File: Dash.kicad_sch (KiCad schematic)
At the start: 120 parts, among them J1 Conn_01x03_Socket, J10 Conn_01x03_Socket, J11 Conn_01x04_Socket, J2 Conn_01x03_Socket, J3 Conn_01x03_Socket, J4 Conn_01x03_Socket, J5 Conn_01x03_Socket, J6 Conn_01x03_Socket, J7 Conn_01x07_Socket, J8 Conn_01x06_Socket, J9 Conn_01x05_Socket, Q1 2N7000, Q10 NPN, Q11 NPN, Q12 NPN, Q13 NPN, Q14 NPN, Q15 NPN, Q16 NPN, Q2 NPN, Q3 NPN, Q4 NPN, Q5 NPN, Q6 NPN, Q7 NPN, Q8 NPN, Q9 NPN, SW1 SW_Push, U1 SFH617A-1, U2 24C02Cx-x-SN, U3 24C02Cx-x-SN, U4 LM2678T-3.3, U5 LM2678T-5.0, U6 ESP32-S2-DevKitM

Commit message: Update Dash.kicad_sch
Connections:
- net Brake Out is gone; now on net Brake Adjusted: Q14.1 (C), R41.1
- net Headlights High Out is gone; now on net Headlights High Adjusted: Q8.1 (C), R29.1
- net Headlights Low Out is gone; now on net Headlights Low Adjusted: Q3.1 (C), R45.1
- net Left Turn Out is gone; now on net Left Turn Adjusted: Q9.1 (C), R30.1
- net Right Turn Out is gone; now on net Right Turn Adjusted: Q10.1 (C), R46.1
- net Speed Out is gone; now on net Speed Adjusted: Q5.1 (C), R24.1
- net Tach Out is gone; now on net Tach Adjusted: Q2.1 (C), R10.1
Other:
- moved on the sheet: Q10, Q11, Q12, Q13, Q14, Q15, Q2, Q3, Q4, Q5, Q6, Q7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

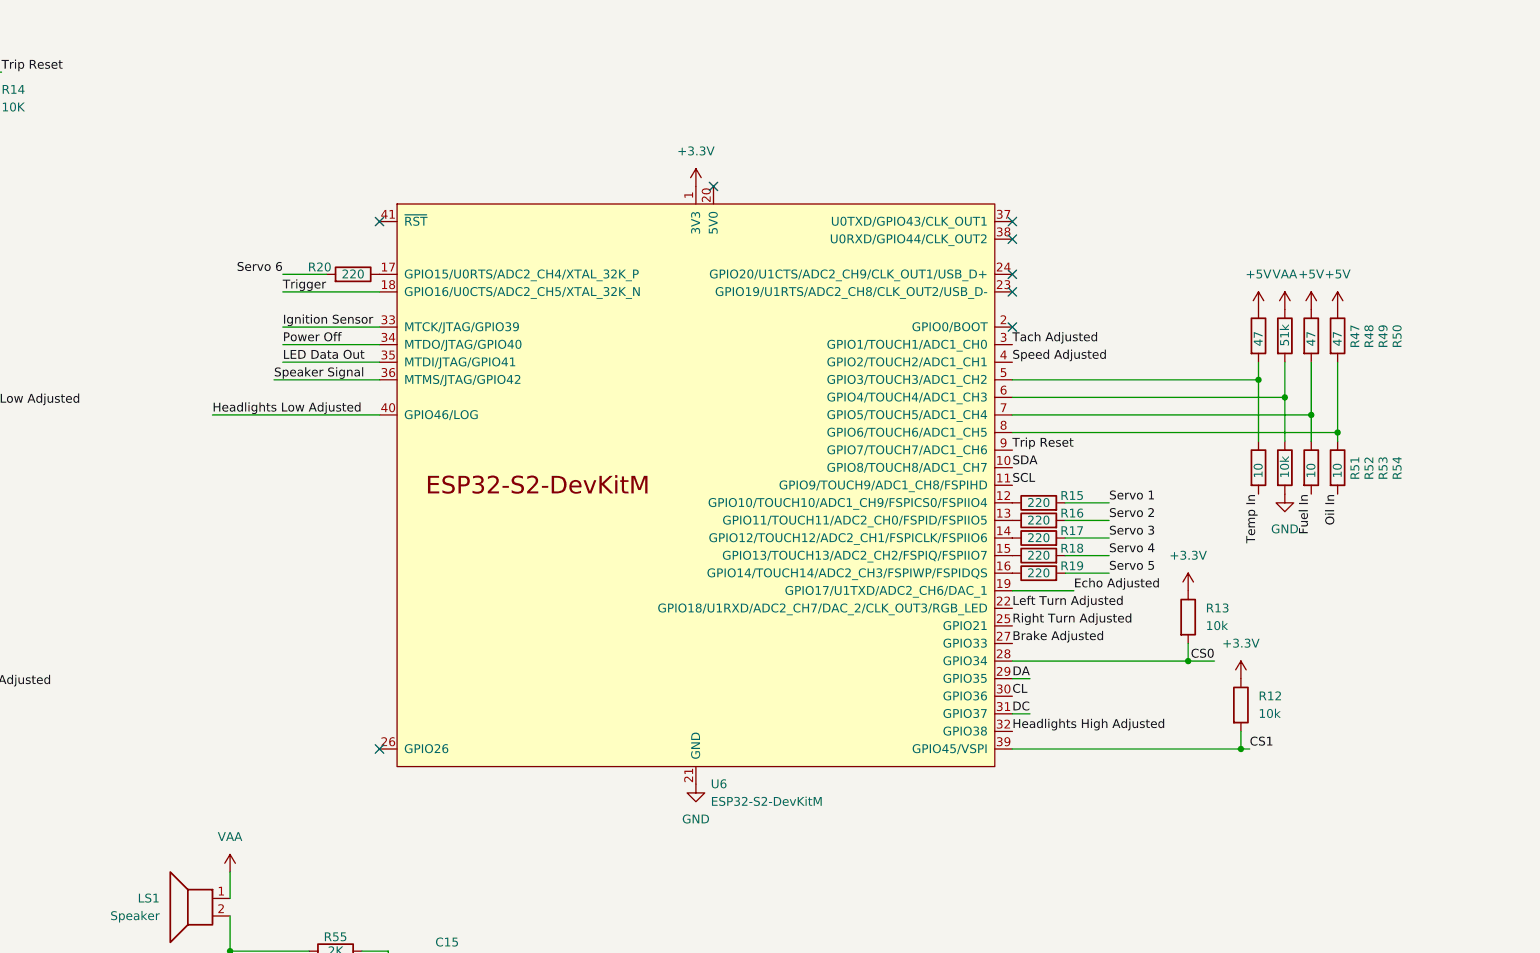
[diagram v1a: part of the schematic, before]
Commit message: added potentiometers
Added potentiometers  to test gauges to the schematic.
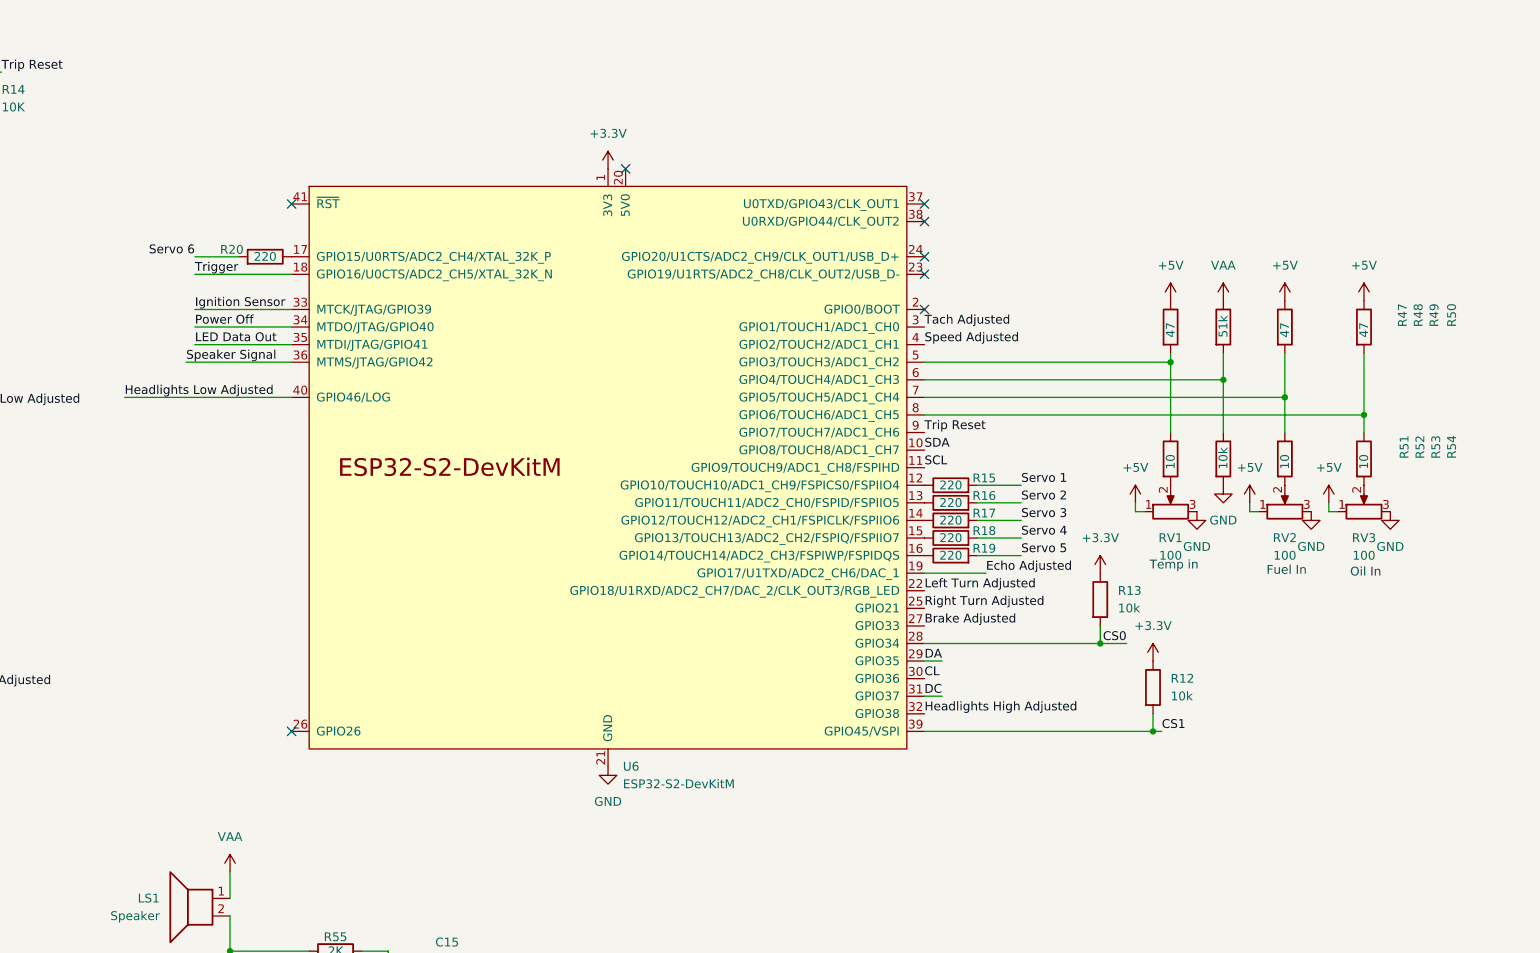
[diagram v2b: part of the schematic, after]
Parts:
- added RV1, RV2, RV3: 100, symbol Device:R_Potentiometer
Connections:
- net +5V: now also RV1.1, RV2.1, RV3.1
- net Fuel In: no longer R53.2
- net GND: now also RV1.3, RV2.3, RV3.3
- net Oil In: no longer R54.2
- net Temp In: no longer R51.2
- new net: R51.2, RV1.2
- new net: R53.2, RV2.2
- new net: R54.2, RV3.2
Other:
- note added: "Fuel In"
- note added: "Oil In"
- note added: "Temp in"
- moved on the sheet: R12, R13, R15, R16, R17, R18, R19, R20, U6

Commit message: Updated resistor values
Changed resistor values on potentiometers to prevent accidental over voltage on gpio pins
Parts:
- R47, R49, R50: value 47 -> 62
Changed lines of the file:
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@@
 			)
 		)
-		(property "Value" "47"
+		(property "Value" "62"
 			(at 381 169.164 90)
 			(show_name no)
@@
 			)
 		)
-		(property "Value" "47"
+		(property "Value" "62"
 			(at 353.06 169.164 90)
 			(show_name no)
@@
 			)
 		)
-		(property "Value" "47"
+		(property "Value" "62"
 			(at 369.57 169.164 90)
 			(show_name no)

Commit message: Update Dash.kicad_sch
Added external ADC. Added hazard logic shifter. Removed unused 3.3V converter.
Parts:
- removed C1: 0.01uF, Capacitor_THT:C_Disc_D3.0mm_W1.6mm_P2.50mm, symbol Device:C
- removed C2, C3, C4: 15uF, Capacitor_THT:CP_Radial_D5.0mm_P2.50mm, symbol Device:C_Polarized
- removed C5: 0.47uF, Capacitor_THT:C_Disc_D3.0mm_W1.6mm_P2.50mm, symbol Device:C
- removed C6, C7: 180uF, Capacitor_THT:CP_Radial_D5.0mm_P2.50mm, symbol Device:C_Polarized
- removed D10: D_Schottky, Diode_THT:D_A-405_P7.62mm_Horizontal, symbol Device:D_Schottky
- removed L1: 22uH, Inductor_THT:L_Radial_D9.5mm_P5.00mm_Fastron_07HVP, symbol Device:L
- removed U4: LM2678T-3.3, Package_TO_SOT_THT:TO-220-7_P2.54x3.7mm_StaggerOdd_Lead3.8mm_Vertical, symbol Buck-Converter:LM2678T-3.3
- added Q17, Q18: NPN, symbol Simulation_SPICE:NPN
- added R56, R58: 1K, symbol Device:R
- added R57, R59: 10K, symbol Device:R
- added U4: ADS1015IDGS, Package_SO:TSSOP-10_3x3mm_P0.5mm, symbol Analog_ADC:ADS1015IDGS
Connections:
- net +3.3V: now also R59.2
- net +5V: now also U6.20 (5V0), R57.2, U4.8 (VDD)
- net CS1: now also U6.6 (GPIO4/TOUCH4/ADC1_CH3); no longer U6.39 (GPIO45/VSPI)
- net GND: now also Q17.3 (E), Q18.3 (E), U4.1 (ADDR), U4.3 (GND)
- net Headlights Low Adjusted: now also U6.5 (GPIO3/TOUCH3/ADC1_CH2); no longer U6.40 (GPIO46/LOG)
- net SCL: now also U4.10 (SCL)
- net SDA: now also U4.9 (SDA)
- net at R50.2, R54.1: now also U4.7 (AIN3); no longer U6.8 (GPIO6/TOUCH6/ADC1_CH5)
- net at R47.2, R51.1: now also U4.4 (AIN0); no longer U6.5 (GPIO3/TOUCH3/ADC1_CH2)
- net at R49.2, R53.1: now also U4.6 (AIN2); no longer U6.7 (GPIO5/TOUCH5/ADC1_CH4)
- net at R48.2, R52.1: now also U4.5 (AIN1); no longer U6.6 (GPIO4/TOUCH4/ADC1_CH3)
- new net: Q17.2 (B), R56.2
- new net: Q17.1 (C), R57.1, R58.1
- new net: Q18.2 (B), R58.2
- new net Hazard Adjusted: Q18.1 (C), R59.1, U6.7 (GPIO5/TOUCH5/ADC1_CH4)
- new net Hazard In: R56.1
- no-connect marks 11 -> 13
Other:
- note added: "Addr 0x48"
- moved on the sheet: C10, C11, C12, C13, C14, C15, C8, C9, D11, L2, LS1, Q10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

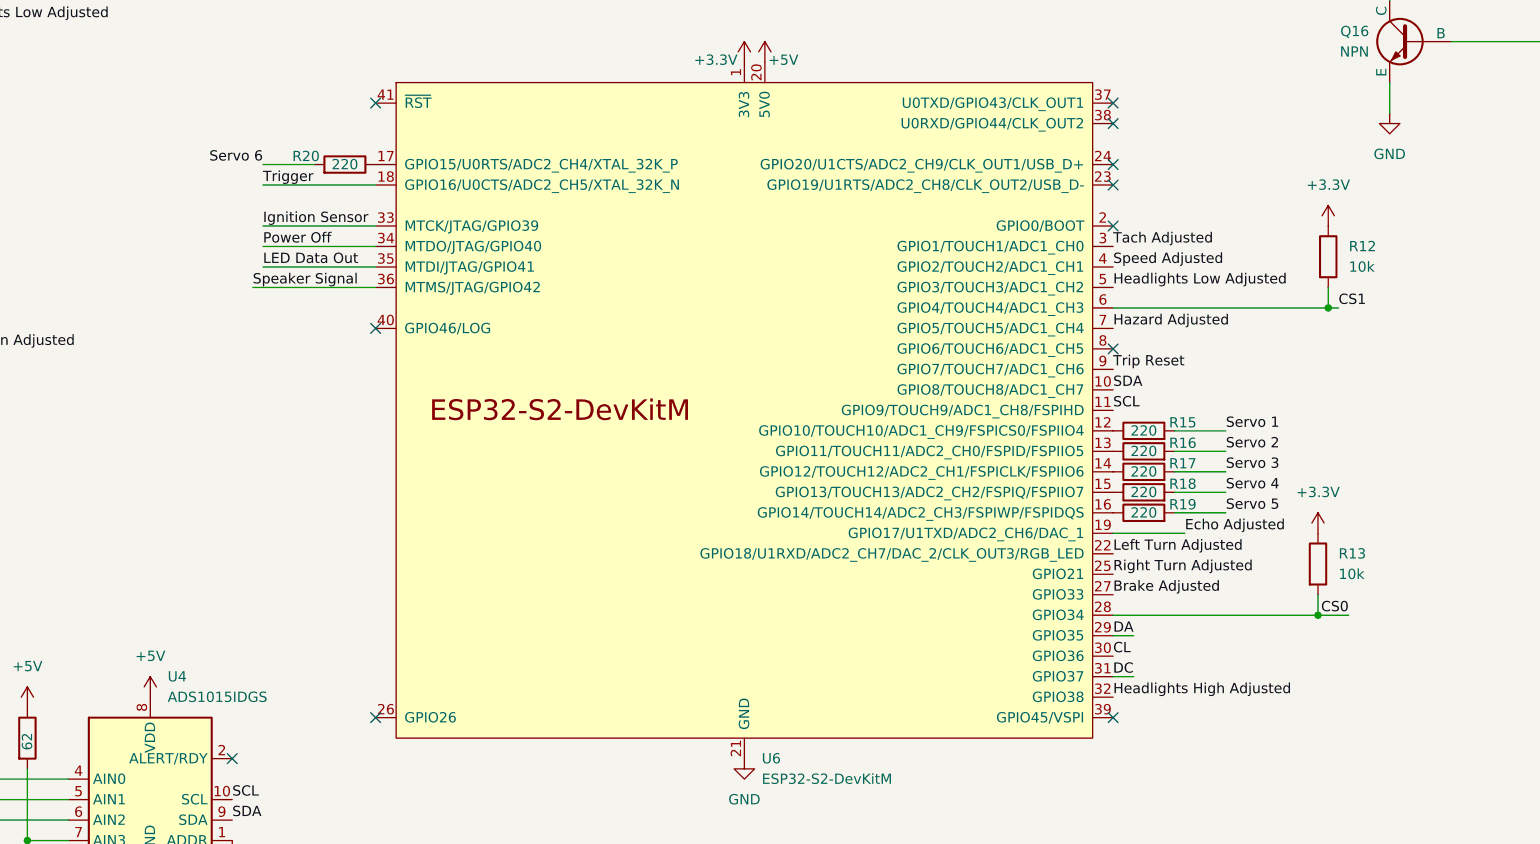
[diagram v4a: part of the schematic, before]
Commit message: Update Dash.kicad_sch
Reassigned pin locations
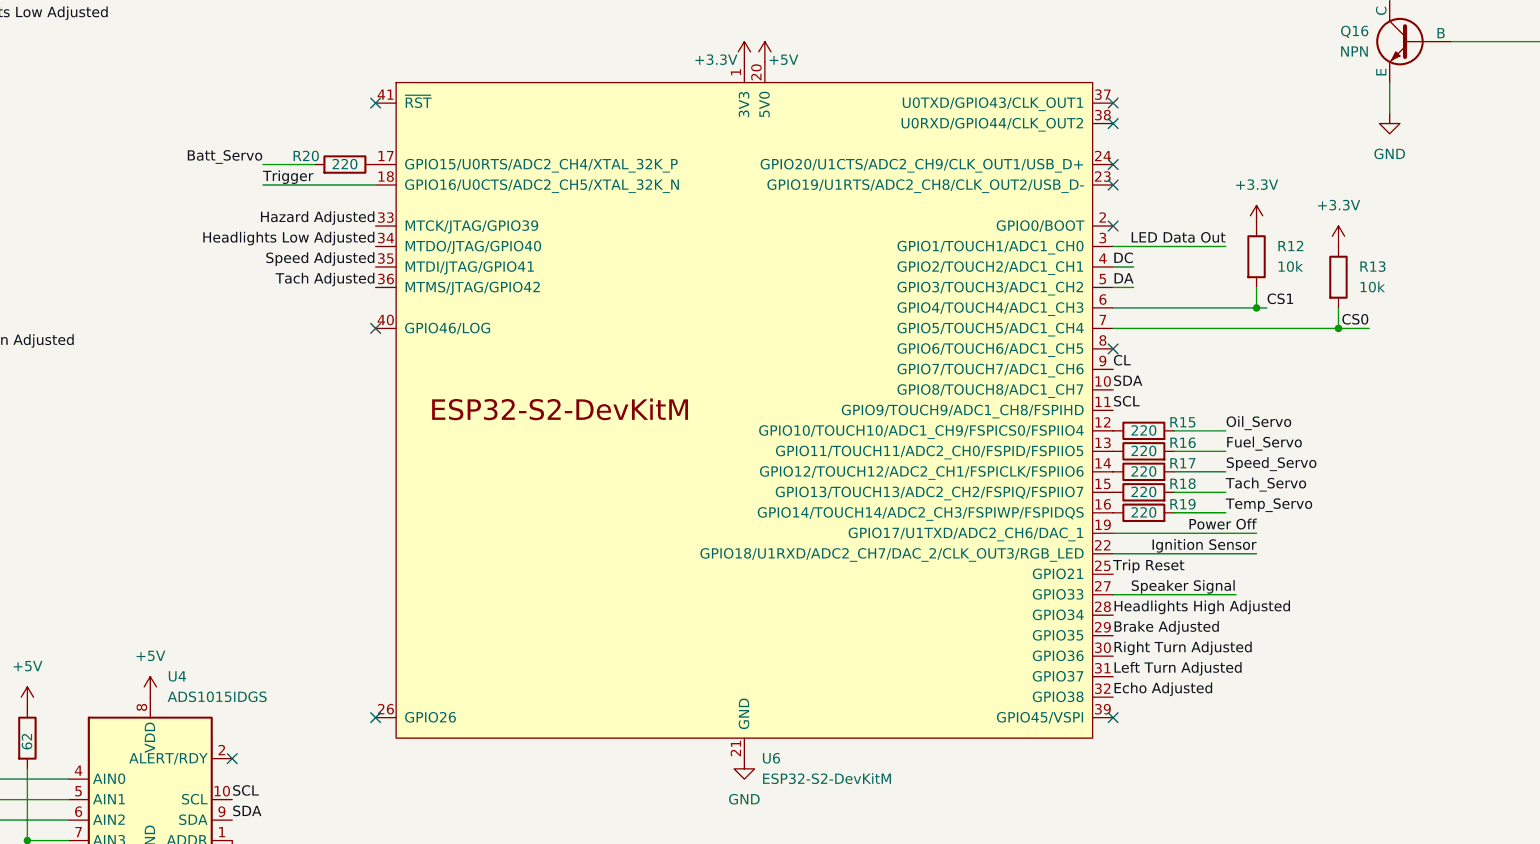
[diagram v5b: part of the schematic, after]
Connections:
- net Brake Adjusted: now also U6.29 (GPIO35); no longer U6.27 (GPIO33)
- net CL: now also U6.9 (GPIO7/TOUCH7/ADC1_CH6); no longer U6.30 (GPIO36)
- net CS0: now also U6.7 (GPIO5/TOUCH5/ADC1_CH4); no longer U6.28 (GPIO34)
- net DA: now also U6.5 (GPIO3/TOUCH3/ADC1_CH2); no longer U6.29 (GPIO35)
- net DC: now also U6.4 (GPIO2/TOUCH2/ADC1_CH1); no longer U6.31 (GPIO37)
- net Echo Adjusted: now also U6.32 (GPIO38); no longer U6.19 (GPIO17/U1TXD/ADC2_CH6/DAC_1)
- net Hazard Adjusted: now also U6.33 (MTCK/JTAG/GPIO39); no longer U6.7 (GPIO5/TOUCH5/ADC1_CH4)
- net Headlights High Adjusted: now also U6.28 (GPIO34); no longer U6.32 (GPIO38)
- net Headlights Low Adjusted: now also U6.34 (MTDO/JTAG/GPIO40); no longer U6.5 (GPIO3/TOUCH3/ADC1_CH2)
- net Ignition Sensor: now also U6.22 (GPIO18/U1RXD/ADC2_CH7/DAC_2/CLK_OUT3/RGB_LED); no longer U6.33 (MTCK/JTAG/GPIO39)
- net LED Data Out: now also U6.3 (GPIO1/TOUCH1/ADC1_CH0); no longer U6.35 (MTDI/JTAG/GPIO41)
- net Left Turn Adjusted: now also U6.31 (GPIO37); no longer U6.22 (GPIO18/U1RXD/ADC2_CH7/DAC_2/CLK_OUT3/RGB_LED)
- net Power Off: now also U6.19 (GPIO17/U1TXD/ADC2_CH6/DAC_1); no longer U6.34 (MTDO/JTAG/GPIO40)
- net Right Turn Adjusted: now also U6.30 (GPIO36); no longer U6.25 (GPIO21)
- net Servo 1: no longer R15.2
- net Servo 2: no longer R16.2
- net Servo 3: no longer R17.2
- net Servo 4: no longer R18.2
- net Servo 5: no longer R19.2
- net Servo 6: no longer R20.2
- net Speaker Signal: now also U6.27 (GPIO33); no longer U6.36 (MTMS/JTAG/GPIO42)
- net Speed Adjusted: now also U6.35 (MTDI/JTAG/GPIO41); no longer U6.4 (GPIO2/TOUCH2/ADC1_CH1)
- net Tach Adjusted: now also U6.36 (MTMS/JTAG/GPIO42); no longer U6.3 (GPIO1/TOUCH1/ADC1_CH0)
- net Trip Reset: now also U6.25 (GPIO21); no longer U6.9 (GPIO7/TOUCH7/ADC1_CH6)
- new net Batt_Servo: R20.2
- new net Fuel_Servo: R16.2
- new net Oil_Servo: R15.2
- new net Speed_Servo: R17.2
- new net Tach_Servo: R18.2
- new net Temp_Servo: R19.2
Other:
- moved on the sheet: R12, R13
